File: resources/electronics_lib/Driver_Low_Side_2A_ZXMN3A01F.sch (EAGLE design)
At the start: 2 parts, among them Q1 ZXMN3A01F

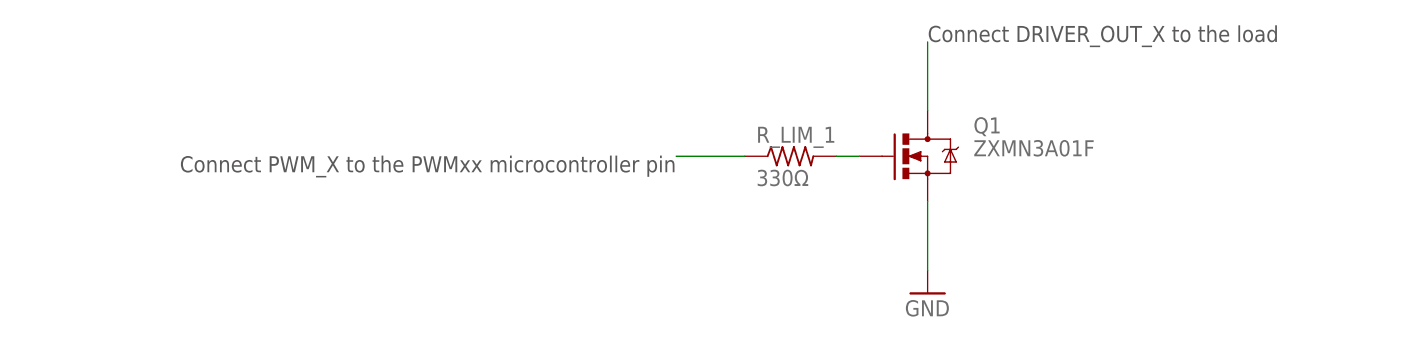
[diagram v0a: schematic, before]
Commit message: Updated driver schematic.
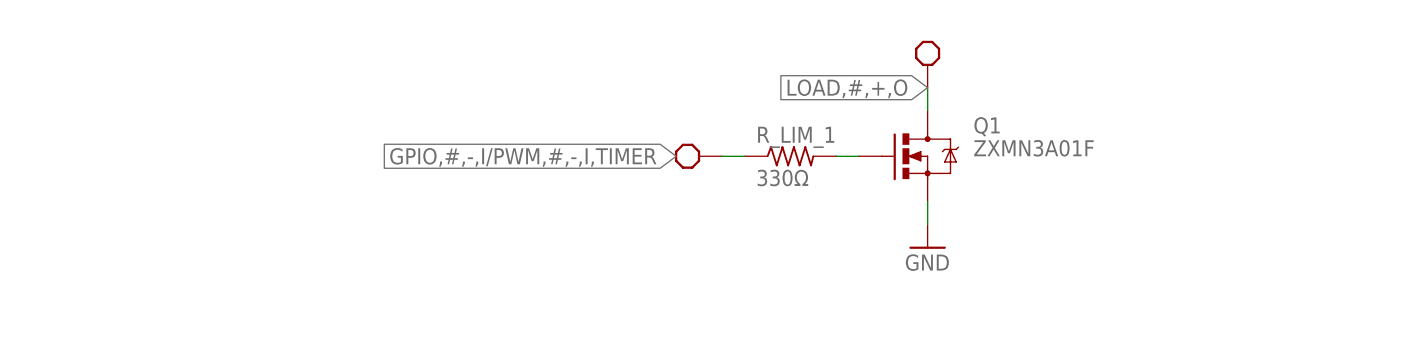
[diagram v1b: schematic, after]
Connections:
- net DRIVER_OUT_1 renamed LOAD,#,+,O
- net PWM_1 renamed GPIO,#,-,I/PWM,#,-,I,TIMER
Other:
- note removed: "Connect DRIVER_OUT_X to the load"
- note removed: "Connect PWM_X to the PWMxx microcontroller pin"
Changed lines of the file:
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@@
 <?xml version="1.0" encoding="utf-8"?>
 <!DOCTYPE eagle SYSTEM "eagle.dtd">
-<eagle version="6.4">
+<eagle version="6.5.0">
 <drawing>
 <settings>
@@
 <layer number="97" name="Info" color="7" fill="1" visible="yes" active="yes"/>
 <layer number="98" name="Guide" color="6" fill="1" visible="yes" active="yes"/>
+<layer number="99" name="SpiceOrder" color="5" fill="1" visible="yes" active="yes"/>
 <layer number="100" name="Muster" color="7" fill="1" visible="no" active="no"/>
 <layer number="101" name="Patch_Top" color="12" fill="4" visible="yes" active="yes"/>
@@
 <part name="R_LIM_1" library="resistor" deviceset="R-US_" device="R0603" value="330Ω"/>
 <part name="GND1" library="supply1" deviceset="GND" device=""/>
+<part name="U$1" library="block_parts" deviceset="BLOCK_REQUIREMENT" device=""/>
+<part name="U$2" library="block_parts" deviceset="BLOCK_REQUIREMENT" device=""/>
 </parts>
 <sheets>
@@
 &lt;p&gt;Connect DRIVER_OUT_X to load&lt;/p&gt;</description>
 <plain>
-<text x="48.26" y="58.42" size="1.778" layer="97" rot="R180">Connect PWM_X to the PWMxx microcontroller pin</text>
-<text x="76.2" y="71.12" size="1.778" layer="97">Connect DRIVER_OUT_X to the load</text>
 </plain>
 <instances>
 <instance part="Q1" gate="G$1" x="76.2" y="58.42"/>
 <instance part="R_LIM_1" gate="G$1" x="60.96" y="58.42"/>
-<instance part="GND1" gate="1" x="76.2" y="43.18"/>
+<instance part="GND1" gate="1" x="76.2" y="48.26"/>
+<instance part="U$1" gate="G$1" x="53.34" y="58.42" rot="R180"/>
+<instance part="U$2" gate="G$1" x="76.2" y="66.04" rot="R90"/>
 </instances>
 <busses>
@@
 </segment>
 </net>
-<net name="DRIVER_OUT_1" class="0">
+<net name="LOAD,#,+,O" class="0">
 <segment>
 <pinref part="Q1" gate="G$1" pin="D"/>
-<wire x1="76.2" y1="71.12" x2="76.2" y2="63.5" width="0.1524" layer="91"/>
+<wire x1="76.2" y1="66.04" x2="76.2" y2="63.5" width="0.1524" layer="91"/>
+<pinref part="U$2" gate="G$1" pin="BLOCK_REQUIREMENT"/>
+<label x="76.2" y="66.04" size="1.778" layer="95" rot="R180" xref="yes"/>
 </segment>
 </net>
@@
 <segment>
 <pinref part="Q1" gate="G$1" pin="S"/>
-<wire x1="76.2" y1="53.34" x2="76.2" y2="45.72" width="0.1524" layer="91"/>
+<wire x1="76.2" y1="53.34" x2="76.2" y2="50.8" width="0.1524" layer="91"/>
 <pinref part="GND1" gate="1" pin="GND"/>
 </segment>
 </net>
-<net name="PWM_1" class="0">
+<net name="GPIO,#,-,I/PWM,#,-,I,TIMER" class="0">
 <segment>
 <pinref part="R_LIM_1" gate="G$1" pin="1"/>
-<wire x1="55.88" y1="58.42" x2="48.26" y2="58.42" width="0.1524" layer="91"/>
+<wire x1="55.88" y1="58.42" x2="53.34" y2="58.42" width="0.1524" layer="91"/>
+<pinref part="U$1" gate="G$1" pin="BLOCK_REQUIREMENT"/>
+<label x="48.26" y="58.42" size="1.778" layer="95" rot="R180" xref="yes"/>
 </segment>
 </net>

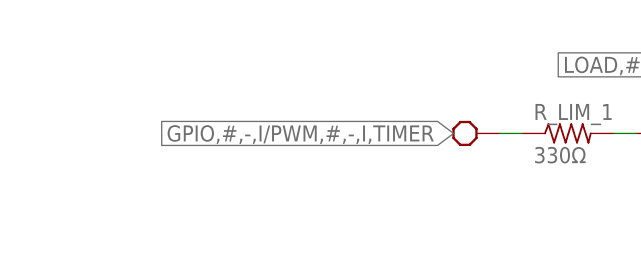
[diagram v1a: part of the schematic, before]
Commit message: Updated Electronics Block Library.
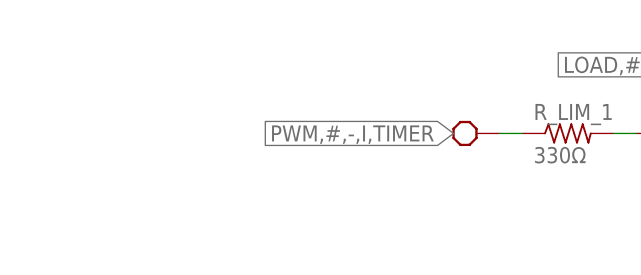
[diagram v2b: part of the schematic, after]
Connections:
- net GPIO,#,-,I/PWM,#,-,I,TIMER renamed PWM,#,-,I,TIMER
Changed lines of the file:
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@@
 </segment>
 </net>
-<net name="GPIO,#,-,I/PWM,#,-,I,TIMER" class="0">
+<net name="PWM,#,-,I,TIMER" class="0">
 <segment>
 <pinref part="R_LIM_1" gate="G$1" pin="1"/>
